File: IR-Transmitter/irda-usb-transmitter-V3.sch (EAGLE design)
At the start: 24 parts, among them IC1 7805, Q2 7.3728MHz, U1 FT232RL, U2 MCP2120

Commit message: Changed size of IR_Transmitter to fit dirtypcbs.com 50x50mm size.
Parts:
- removed C4: 100n, rcl:C-EUC1206
- removed C5: 4µ7, rcl:CPOL-EUE2.5-6
- removed LED_STAT+, LED_STAT-: IR-LED, wirepad:WIREPADSMD5-2,5
- removed U1: FT232RL, ftdichip-3:FT232RL
- IC1: value 7805 -> FT232RL; device 78xx_with_heatsink:78XXH -> ftdichip-3:FT232RL
- renumbered U2 to IC2, X1 to USB
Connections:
- net +12V: no longer IC1.IN, LED_STAT+.P
- net +3V3: now also IC1.3V3OUT; no longer U1.3V3OUT
- net D+: now also IC1.USBDP; no longer U1.USBDP
- net D-: now also IC1.USBDM; no longer U1.USBDM
- net GND: now also IC1.AGND, IC1.GND1, IC1.GND2, IC1.GND3, IC1.TEST; no longer C4.2, C5.-, IC1.GND, U1.AGND, U1.GND1, U1.GND2, U1.GND3, U1.TEST
- net IRLEDS-: no longer LED_STAT-.P
- net N$3: now also IC1.DSR#, IC1.DTR#; no longer U1.DSR#, U1.DTR#
- net RX: now also IC1.RXD; no longer U1.RXD
- net TX: now also IC1.TXD; no longer U1.TXD
- net VCC: now also IC1.RESET#, IC1.VCC, IC1.VCCIO, USB.VBUS; no longer C4.1, C5.+, IC1.OUT, U1.RESET#, U1.VCC, U1.VCCIO
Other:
- note added: "v3.0.1"
- note removed: "Version 1.0"
- moved on the sheet: C3, C6, GND, LED+

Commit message: Added a jumper to switch between USB power and extranl power for IR-Transmitter. Updated README.md
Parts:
- added JP1: (no value), pinhead:PINHD-2X2
- renumbered 12V to V+
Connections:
- removed net +12V: C3.1, C6.+, LED+.P, V+.P
- new net V+: C3.1, C6.+, JP1.3, V+.P
- new net VCCIO: IC1.RESET#, IC1.VCC, IC1.VCCIO, IC2.BAUD2, IC2.EN, IC2.MODE, IC2.RESET, IC2.VDD, JP1.1, USB.VBUS
- net VCC: now also JP1.2, JP1.4, LED+.P; no longer IC1.RESET#, IC1.VCC, IC1.VCCIO, IC2.BAUD2, IC2.EN, IC2.MODE, IC2.RESET, IC2.VDD, USB.VBUS

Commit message: Added optional resistors R2  & R3 to schematics and layout.
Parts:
- added R2, R3: (no value), rcl:R-EU_R1206
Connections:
- new net N$1: LED+.P, R2.1, R3.2
- net IRLEDS-: now also R3.1
- net VCC: now also R2.2; no longer LED+.P
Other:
- note added: "v3.0.2"
- note removed: "v3.0.1"
- moved on the sheet: JP1
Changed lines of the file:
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@@
 <part name="SUPPLY2" library="supply2" deviceset="V+" device=""/>
 <part name="VCC1" library="supply1" deviceset="VCCIO" device=""/>
+<part name="R2" library="rcl" deviceset="R-EU_" device="R1206"/>
+<part name="R3" library="rcl" deviceset="R-EU_" device="R1206"/>
 </parts>
 <sheets>
 <sheet>
 <plain>
-<text x="215.9" y="20.32" size="2.54" layer="94">v3.0.1</text>
+<text x="215.9" y="20.32" size="2.54" layer="94">v3.0.2</text>
 <text x="162.56" y="20.32" size="2.54" layer="94">NorthernStars</text>
 <text x="162.56" y="17.78" size="1.778" layer="94">FH Kiel -Fachbereich IuE</text>
@@
 <instance part="+3V2" gate="G$1" x="50.8" y="152.4"/>
 <instance part="GND2" gate="1" x="50.8" y="119.38"/>
-<instance part="JP1" gate="A" x="73.66" y="91.44"/>
-<instance part="P+4" gate="VCC" x="83.82" y="106.68"/>
+<instance part="JP1" gate="A" x="81.28" y="88.9"/>
+<instance part="P+4" gate="VCC" x="91.44" y="104.14"/>
 <instance part="VCC2" gate="G$1" x="83.82" y="152.4"/>
 <instance part="VCC3" gate="G$1" x="96.52" y="152.4"/>
@@
 <instance part="VCC6" gate="G$1" x="152.4" y="63.5"/>
 <instance part="SUPPLY1" gate="1" x="33.02" y="111.76"/>
-<instance part="P+1" gate="VCC" x="218.44" y="137.16"/>
-<instance part="SUPPLY2" gate="1" x="53.34" y="109.22"/>
-<instance part="VCC1" gate="G$1" x="60.96" y="109.22"/>
+<instance part="P+1" gate="VCC" x="218.44" y="144.78"/>
+<instance part="SUPPLY2" gate="1" x="60.96" y="106.68"/>
+<instance part="VCC1" gate="G$1" x="68.58" y="106.68"/>
+<instance part="R2" gate="G$1" x="218.44" y="132.08" rot="R90"/>
+<instance part="R3" gate="G$1" x="218.44" y="116.84" rot="R90"/>
 </instances>
 <busses>
@@
 <pinref part="LED-" gate="G$1" pin="P"/>
 <pinref part="U$1" gate="G$1" pin="P$2"/>
+<pinref part="R3" gate="G$1" pin="1"/>
+<junction x="218.44" y="111.76"/>
 </segment>
 </net>
@@
 <pinref part="JP1" gate="A" pin="1"/>
 <pinref part="VCC1" gate="G$1" pin="VCCIO"/>
-<wire x1="68.58" y1="93.98" x2="60.96" y2="93.98" width="0.1524" layer="91"/>
-<wire x1="60.96" y1="93.98" x2="60.96" y2="106.68" width="0.1524" layer="91"/>
+<wire x1="76.2" y1="91.44" x2="68.58" y2="91.44" width="0.1524" layer="91"/>
+<wire x1="68.58" y1="91.44" x2="68.58" y2="104.14" width="0.1524" layer="91"/>
 </segment>
 </net>
@@
 <pinref part="JP1" gate="A" pin="3"/>
 <pinref part="SUPPLY2" gate="1" pin="V+"/>
-<wire x1="68.58" y1="91.44" x2="53.34" y2="91.44" width="0.1524" layer="91"/>
-<wire x1="53.34" y1="91.44" x2="53.34" y2="106.68" width="0.1524" layer="91"/>
+<wire x1="76.2" y1="88.9" x2="60.96" y2="88.9" width="0.1524" layer="91"/>
+<wire x1="60.96" y1="88.9" x2="60.96" y2="104.14" width="0.1524" layer="91"/>
 </segment>
 </net>
 <net name="VCC" class="0">
-<segment>
-<wire x1="233.68" y1="121.92" x2="218.44" y2="121.92" width="0.1524" layer="91"/>
-<wire x1="218.44" y1="121.92" x2="218.44" y2="134.62" width="0.1524" layer="91"/>
-<pinref part="LED+" gate="G$1" pin="P"/>
-<pinref part="P+1" gate="VCC" pin="VCC"/>
-</segment>
 <segment>
 <pinref part="JP1" gate="A" pin="2"/>
 <pinref part="P+4" gate="VCC" pin="VCC"/>
-<wire x1="76.2" y1="93.98" x2="83.82" y2="93.98" width="0.1524" layer="91"/>
-<wire x1="83.82" y1="93.98" x2="83.82" y2="104.14" width="0.1524" layer="91"/>
+<wire x1="83.82" y1="91.44" x2="91.44" y2="91.44" width="0.1524" layer="91"/>
+<wire x1="91.44" y1="91.44" x2="91.44" y2="101.6" width="0.1524" layer="91"/>
 <pinref part="JP1" gate="A" pin="4"/>
-<wire x1="76.2" y1="91.44" x2="83.82" y2="91.44" width="0.1524" layer="91"/>
-<wire x1="83.82" y1="91.44" x2="83.82" y2="93.98" width="0.1524" layer="91"/>
-<junction x="83.82" y="93.98"/>
-</segment>
-</net>
+<wire x1="83.82" y1="88.9" x2="91.44" y2="88.9" width="0.1524" layer="91"/>
+<wire x1="91.44" y1="88.9" x2="91.44" y2="91.44" width="0.1524" layer="91"/>
+<junction x="91.44" y="91.44"/>
+</segment>
+<segment>
+<pinref part="P+1" gate="VCC" pin="VCC"/>
+<pinref part="R2" gate="G$1" pin="2"/>
+<wire x1="218.44" y1="137.16" x2="218.44" y2="142.24" width="0.1524" layer="91"/>
+</segment>
+</net>
+<net name="N$1" class="0">
+<segment>
+<pinref part="LED+" gate="G$1" pin="P"/>
+<pinref part="R2" gate="G$1" pin="1"/>
+<wire x1="233.68" y1="121.92" x2="218.44" y2="121.92" width="0.1524" layer="91"/>
+<wire x1="218.44" y1="121.92" x2="218.44" y2="127" width="0.1524" layer="91"/>
+<pinref part="R3" gate="G$1" pin="2"/>
+<junction x="218.44" y="121.92"/>
+</segment>
+</net>

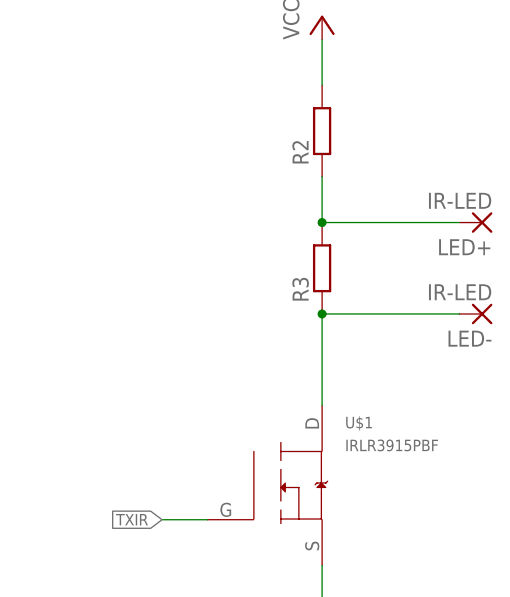
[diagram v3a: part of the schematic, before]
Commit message: Updated Board layouts an schematics
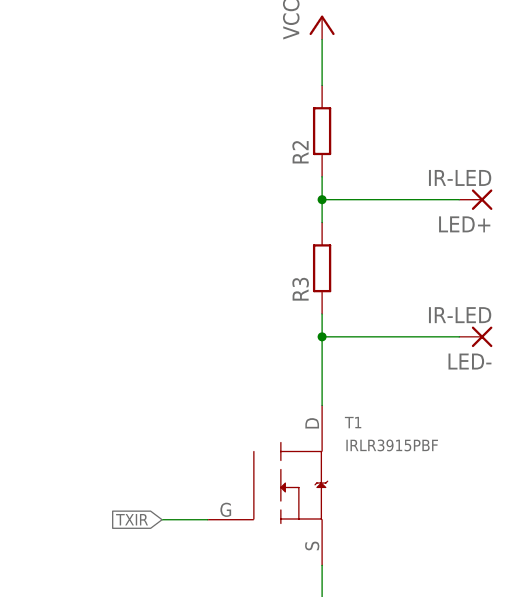
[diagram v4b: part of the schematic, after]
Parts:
- renumbered U$1 to T1
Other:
- moved on the sheet: LED+, LED-
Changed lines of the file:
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@@
 <?xml version="1.0" encoding="utf-8"?>
 <!DOCTYPE eagle SYSTEM "eagle.dtd">
-<eagle version="6.3">
+<eagle version="7.2.0">
 <drawing>
 <settings>
@@
 <part name="H3" library="holes" deviceset="MOUNT-HOLE" device="2.8"/>
 <part name="H4" library="holes" deviceset="MOUNT-HOLE" device="2.8"/>
-<part name="U$1" library="international" deviceset="IRLR3915PBF" device=""/>
+<part name="T1" library="international" deviceset="IRLR3915PBF" device=""/>
 <part name="GND14" library="supply1" deviceset="GND" device=""/>
 <part name="IC2" library="microchip" deviceset="MCP2120" device=""/>
@@
 <instance part="H3" gate="G$1" x="20.32" y="27.94"/>
 <instance part="H4" gate="G$1" x="20.32" y="20.32"/>
-<instance part="U$1" gate="G$1" x="213.36" y="93.98"/>
+<instance part="T1" gate="G$1" x="213.36" y="93.98"/>
 <instance part="GND14" gate="1" x="33.02" y="78.74"/>
 <instance part="IC2" gate="G$1" x="127" y="45.72"/>
 <instance part="GND15" gate="1" x="147.32" y="10.16"/>
-<instance part="LED+" gate="G$1" x="236.22" y="121.92" rot="R180"/>
-<instance part="LED-" gate="G$1" x="236.22" y="111.76" rot="R180"/>
+<instance part="LED+" gate="G$1" x="236.22" y="124.46" rot="R180"/>
+<instance part="LED-" gate="G$1" x="236.22" y="109.22" rot="R180"/>
 <instance part="V+" gate="1" x="22.86" y="99.06"/>
 <instance part="GND" gate="1" x="22.86" y="86.36"/>
@@
 <segment>
 <wire x1="218.44" y1="83.82" x2="218.44" y2="76.2" width="0.1524" layer="91"/>
-<pinref part="U$1" gate="G$1" pin="P$3"/>
+<pinref part="T1" gate="G$1" pin="P$3"/>
 <pinref part="GND7" gate="1" pin="GND"/>
 </segment>
@@
 <net name="IRLEDS-" class="0">
 <segment>
-<wire x1="233.68" y1="111.76" x2="218.44" y2="111.76" width="0.1524" layer="91"/>
-<wire x1="218.44" y1="111.76" x2="218.44" y2="101.6" width="0.1524" layer="91"/>
+<wire x1="218.44" y1="111.76" x2="218.44" y2="109.22" width="0.1524" layer="91"/>
+<pinref part="T1" gate="G$1" pin="P$2"/>
+<pinref part="R3" gate="G$1" pin="1"/>
 <pinref part="LED-" gate="G$1" pin="P"/>
-<pinref part="U$1" gate="G$1" pin="P$2"/>
-<pinref part="R3" gate="G$1" pin="1"/>
-<junction x="218.44" y="111.76"/>
+<wire x1="218.44" y1="109.22" x2="218.44" y2="101.6" width="0.1524" layer="91"/>
+<wire x1="233.68" y1="109.22" x2="218.44" y2="109.22" width="0.1524" layer="91"/>
+<junction x="218.44" y="109.22"/>
 </segment>
 </net>
@@
 <wire x1="200.66" y1="88.9" x2="205.74" y2="88.9" width="0.1524" layer="91"/>
 <label x="200.66" y="88.9" size="1.27" layer="95" rot="R180" xref="yes"/>
-<pinref part="U$1" gate="G$1" pin="G"/>
+<pinref part="T1" gate="G$1" pin="G"/>
 </segment>
 </net>
@@
 <net name="N$1" class="0">
 <segment>
+<pinref part="R2" gate="G$1" pin="1"/>
+<wire x1="218.44" y1="121.92" x2="218.44" y2="124.46" width="0.1524" layer="91"/>
+<pinref part="R3" gate="G$1" pin="2"/>
 <pinref part="LED+" gate="G$1" pin="P"/>
-<pinref part="R2" gate="G$1" pin="1"/>
-<wire x1="233.68" y1="121.92" x2="218.44" y2="121.92" width="0.1524" layer="91"/>
-<wire x1="218.44" y1="121.92" x2="218.44" y2="127" width="0.1524" layer="91"/>
-<pinref part="R3" gate="G$1" pin="2"/>
-<junction x="218.44" y="121.92"/>
-</segment>
-</net>
+<wire x1="218.44" y1="124.46" x2="218.44" y2="127" width="0.1524" layer="91"/>
+<wire x1="233.68" y1="124.46" x2="218.44" y2="124.46" width="0.1524" layer="91"/>
+<junction x="218.44" y="124.46"/>
+</segment>
+</net>

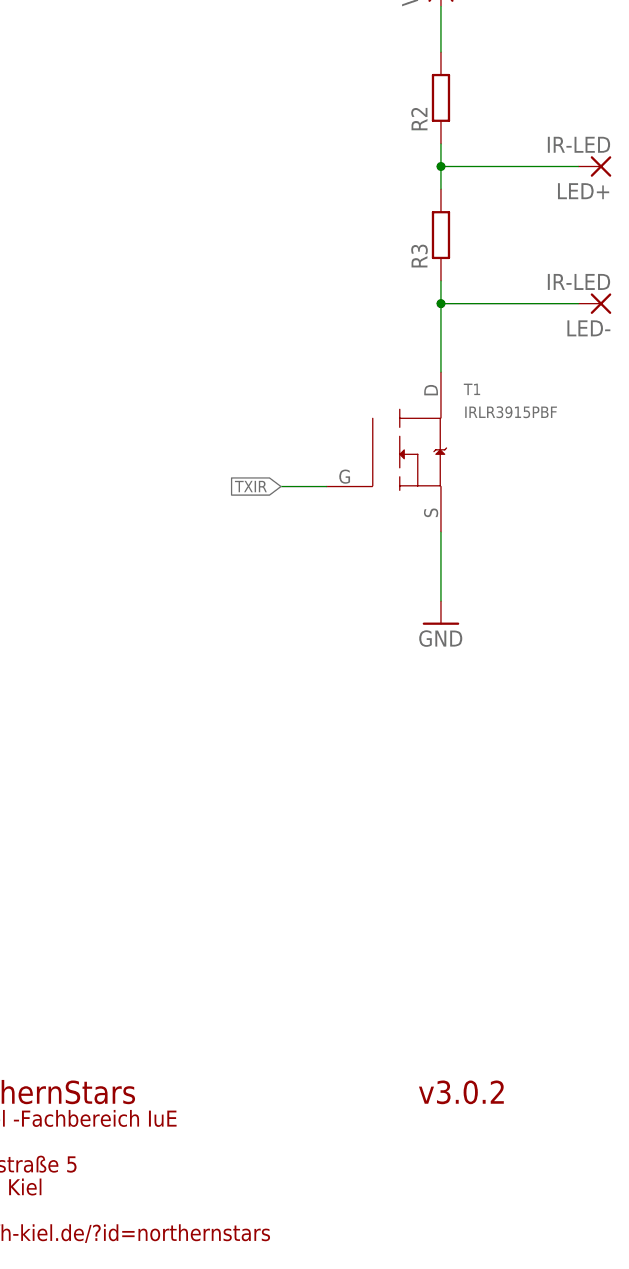
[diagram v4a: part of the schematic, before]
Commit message: Fixed layout errors. Layout is now tested.
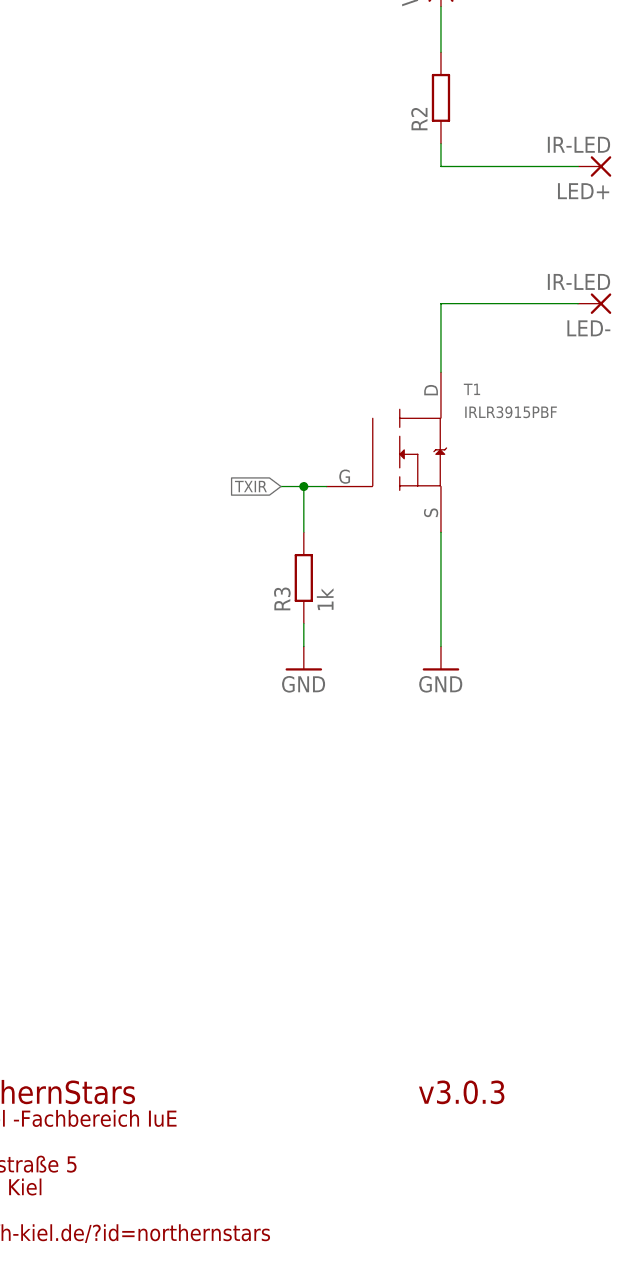
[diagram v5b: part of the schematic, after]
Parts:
- R3: value (none) -> 1k
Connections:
- net GND: now also R3.1
- net IRLEDS-: no longer R3.1
- net N$1: no longer R3.2
- net TXIR: now also R3.2
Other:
- note added: "v3.0.3"
- note removed: "v3.0.2"
- moved on the sheet: R3
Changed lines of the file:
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@@
 <part name="VCC1" library="supply1" deviceset="VCCIO" device=""/>
 <part name="R2" library="rcl" deviceset="R-EU_" device="R1206"/>
-<part name="R3" library="rcl" deviceset="R-EU_" device="R1206"/>
+<part name="R3" library="rcl" deviceset="R-EU_" device="R1206" value="1k"/>
+<part name="GND1" library="supply1" deviceset="GND" device=""/>
 </parts>
 <sheets>
 <sheet>
 <plain>
-<text x="215.9" y="20.32" size="2.54" layer="94">v3.0.2</text>
+<text x="215.9" y="20.32" size="2.54" layer="94">v3.0.3</text>
 <text x="162.56" y="20.32" size="2.54" layer="94">NorthernStars</text>
 <text x="162.56" y="17.78" size="1.778" layer="94">FH Kiel -Fachbereich IuE</text>
@@
 <instance part="C2" gate="G$1" x="101.6" y="22.86"/>
 <instance part="Q2" gate="G$1" x="93.98" y="35.56"/>
-<instance part="GND7" gate="1" x="218.44" y="73.66"/>
+<instance part="GND7" gate="1" x="218.44" y="68.58"/>
 <instance part="+3V1" gate="G$1" x="104.14" y="152.4"/>
 <instance part="GND4" gate="1" x="93.98" y="10.16"/>
@@
 <instance part="VCC1" gate="G$1" x="68.58" y="106.68"/>
 <instance part="R2" gate="G$1" x="218.44" y="132.08" rot="R90"/>
-<instance part="R3" gate="G$1" x="218.44" y="116.84" rot="R90"/>
+<instance part="R3" gate="G$1" x="203.2" y="78.74" rot="R90"/>
+<instance part="GND1" gate="1" x="203.2" y="68.58"/>
 </instances>
 <busses>
@@
 </segment>
 <segment>
-<wire x1="218.44" y1="83.82" x2="218.44" y2="76.2" width="0.1524" layer="91"/>
+<wire x1="218.44" y1="83.82" x2="218.44" y2="71.12" width="0.1524" layer="91"/>
 <pinref part="T1" gate="G$1" pin="P$3"/>
 <pinref part="GND7" gate="1" pin="GND"/>
@@
 <wire x1="50.8" y1="121.92" x2="50.8" y2="134.62" width="0.1524" layer="91"/>
 </segment>
+<segment>
+<pinref part="GND1" gate="1" pin="GND"/>
+<pinref part="R3" gate="G$1" pin="1"/>
+<wire x1="203.2" y1="73.66" x2="203.2" y2="71.12" width="0.1524" layer="91"/>
+</segment>
 </net>
 <net name="D+" class="0">
@@
 <net name="IRLEDS-" class="0">
 <segment>
-<wire x1="218.44" y1="111.76" x2="218.44" y2="109.22" width="0.1524" layer="91"/>
 <pinref part="T1" gate="G$1" pin="P$2"/>
-<pinref part="R3" gate="G$1" pin="1"/>
 <pinref part="LED-" gate="G$1" pin="P"/>
 <wire x1="218.44" y1="109.22" x2="218.44" y2="101.6" width="0.1524" layer="91"/>
 <wire x1="233.68" y1="109.22" x2="218.44" y2="109.22" width="0.1524" layer="91"/>
-<junction x="218.44" y="109.22"/>
 </segment>
 </net>
@@
 </segment>
 <segment>
-<wire x1="200.66" y1="88.9" x2="205.74" y2="88.9" width="0.1524" layer="91"/>
+<wire x1="200.66" y1="88.9" x2="203.2" y2="88.9" width="0.1524" layer="91"/>
 <label x="200.66" y="88.9" size="1.27" layer="95" rot="R180" xref="yes"/>
 <pinref part="T1" gate="G$1" pin="G"/>
+<pinref part="R3" gate="G$1" pin="2"/>
+<wire x1="203.2" y1="88.9" x2="205.74" y2="88.9" width="0.1524" layer="91"/>
+<wire x1="203.2" y1="83.82" x2="203.2" y2="88.9" width="0.1524" layer="91"/>
+<junction x="203.2" y="88.9"/>
 </segment>
 </net>
@@
 <segment>
 <pinref part="R2" gate="G$1" pin="1"/>
-<wire x1="218.44" y1="121.92" x2="218.44" y2="124.46" width="0.1524" layer="91"/>
-<pinref part="R3" gate="G$1" pin="2"/>
 <pinref part="LED+" gate="G$1" pin="P"/>
 <wire x1="218.44" y1="124.46" x2="218.44" y2="127" width="0.1524" layer="91"/>
 <wire x1="233.68" y1="124.46" x2="218.44" y2="124.46" width="0.1524" layer="91"/>
-<junction x="218.44" y="124.46"/>
-</segment>
-</net>
+</segment>
+</net>
